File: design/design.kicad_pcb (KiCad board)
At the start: 2 copper layers, 76.2 x 68.6 mm, 31 parts, among them J1 Conn_01x03_Pin, J2 Conn_01x02_Pin, J3 Conn_01x02_Pin, J4 Conn_01x02_Pin, U1 MC7912, U2 L7812, U3 OPA209AID, U4 TL081, U5 TL081

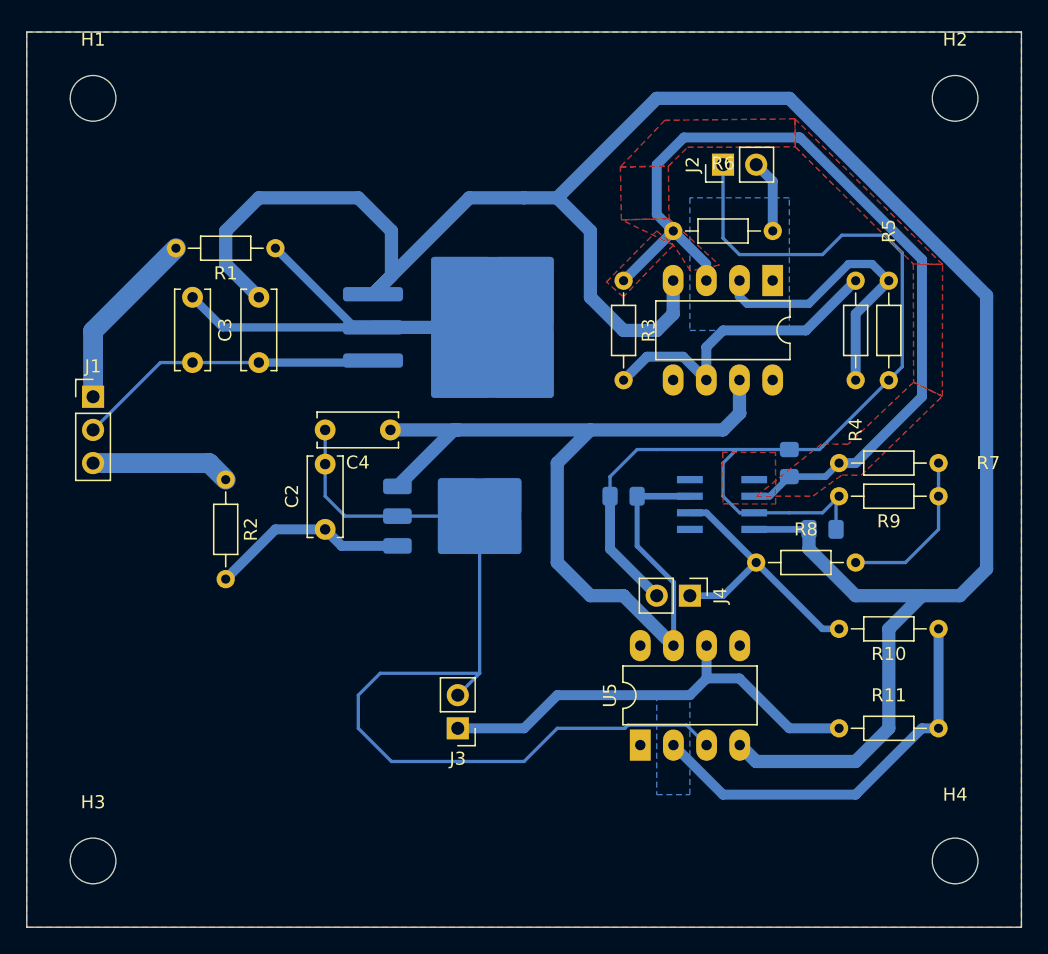
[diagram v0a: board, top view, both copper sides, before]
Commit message: Borre el plano de masa sobre Front Layer F.Cu porque era innecesario.
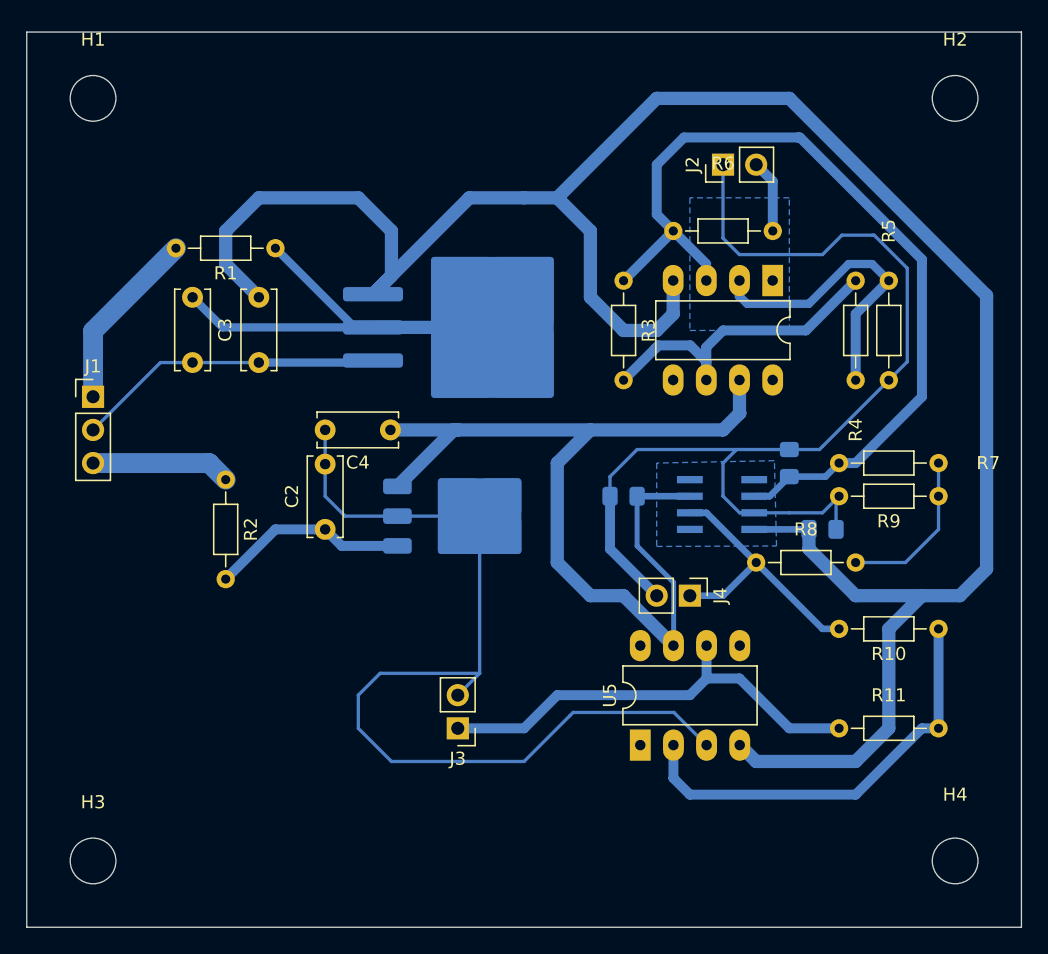
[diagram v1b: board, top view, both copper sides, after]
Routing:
- net Net-(R3-Pad2): track 23.9 -> 25.4 mm
- net Net-(U5--): track 31.6 -> 33.1 mm
- net Earth: track 180.7 -> 181.4 mm
- removed copper zone on F.Cu, net (none)
- removed copper zone on B.Cu, net Earth
- removed copper zone on F.Cu, net Earth

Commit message: Version final, archivos Gerber exportados y enviados
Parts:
- added J5: Conn_01x02_Pin, Connector_PinHeader_2.54mm:PinHeader_1x02_P2.54mm_Vertical, F.Cu at (132.1, 58.4)
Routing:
- net Earth: track 181.4 -> 226.3 mm
- net -12V: track 171.8 -> 189.6 mm
- net Net-(U4--): track 23.3 -> 24.0 mm
- added copper zone on B.Cu, net Earth
